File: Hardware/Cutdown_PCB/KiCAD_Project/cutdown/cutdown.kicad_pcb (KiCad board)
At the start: 4 copper layers, 43.2 x 152.4 mm, 74 parts, among them J1 Mini_USB_B, J2 External Cutdown, J3 ISP, J4 Hot Wire, Q1 2N7002, Q2 FQP30N06L, SW1 SW_SPST, U1 FT231XS, U2 SPX3819M5-L-3-3, U3 ATmega328P-AU, U4 XBee, U5 BMP388, Y1 8MHz

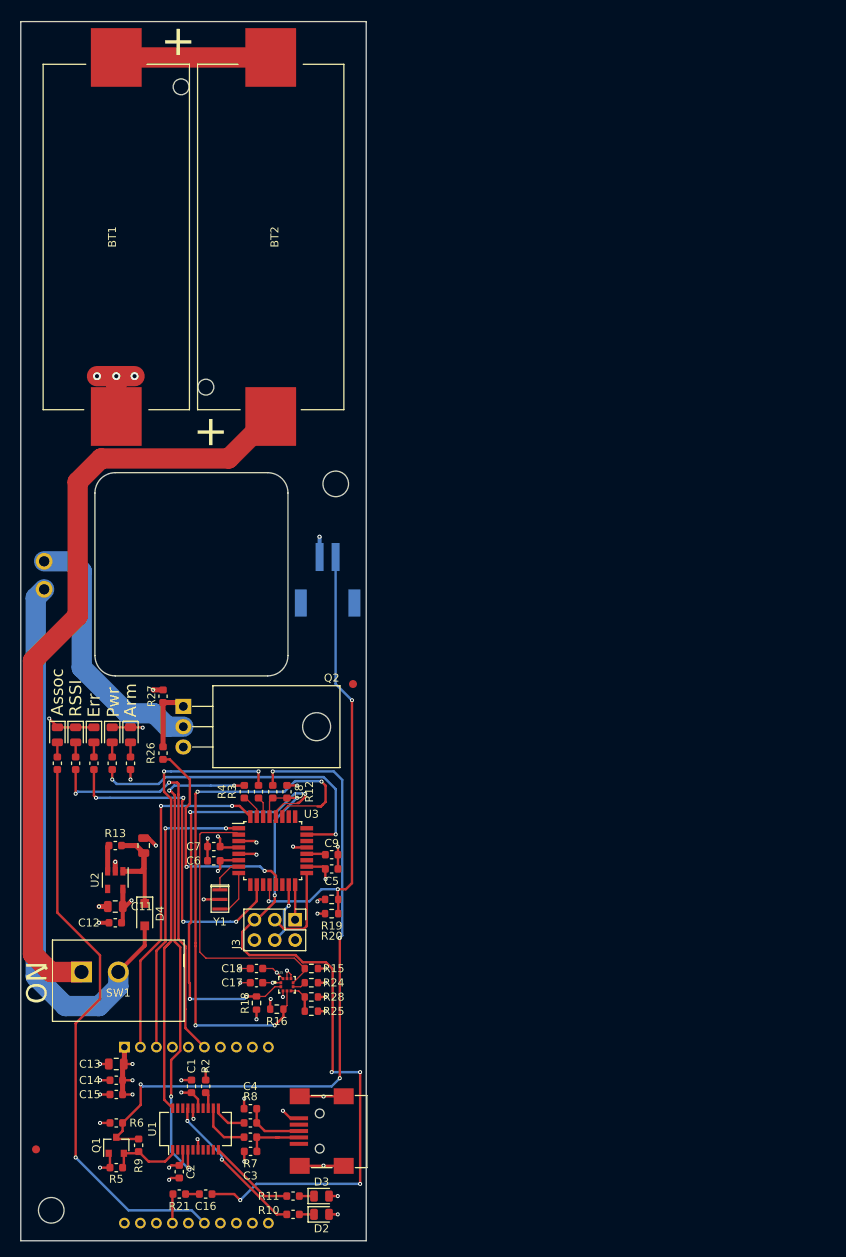
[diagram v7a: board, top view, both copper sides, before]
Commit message: Add Arm LED and improve board layout
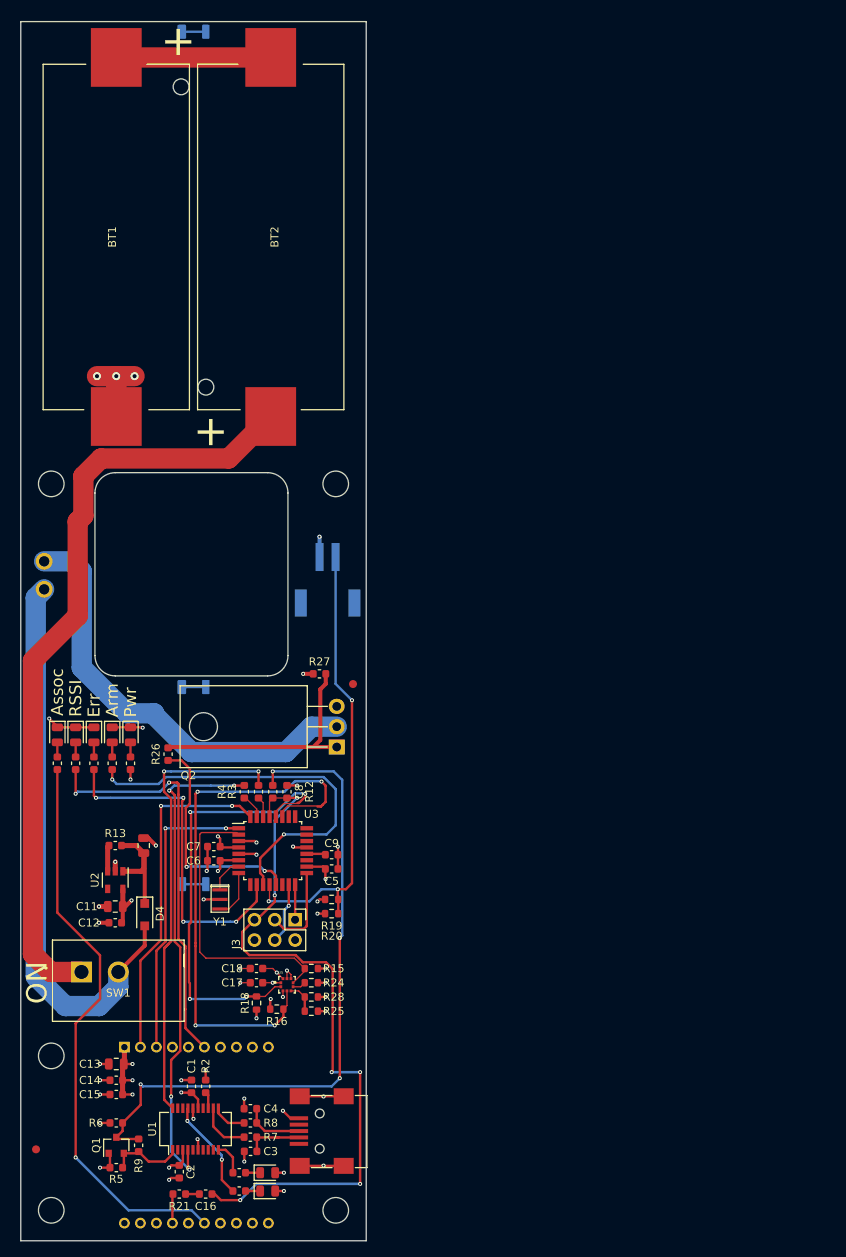
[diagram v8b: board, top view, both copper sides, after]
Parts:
- added H3: M3_ISO_7380, mechanical:MountingHole_3.2mm_M3_ISO7380, F.Cu at (105.9, 82.9)
- added H4: M3_ISO_7380, mechanical:MountingHole_3.2mm_M3_ISO7380, F.Cu at (141.5, 173.7)
- added H5: M3_ISO_7380, mechanical:MountingHole_3.2mm_M3_ISO7380, F.Cu at (105.9, 154.4)
- added TP1: 1-0000952, test_points:1-0000952, B.Cu at (123.7, 26.4)
- added TP2: 1-0000952, test_points:1-0000952, B.Cu at (123.7, 79.8)
- added TP3: 1-0000952, test_points:1-0000952, B.Cu at (123.7, 133.0)
- added TP4: 1-0000952, test_points:1-0000952, B.Cu at (123.7, 108.3)
- moved Q2 19.8 mm to (141.6, 115.8), turned to 90 degrees
- moved R27 19.8 mm to (139.4, 106.7), turned to 180 degrees
- moved D2 7.34 mm to (133.0, 171.3)
- moved D3 7.34 mm to (133.0, 169.0)
- moved R10 7.34 mm to (129.4, 171.3)
- moved R11 7.34 mm to (129.4, 169.0)
- moved R26 0.65 mm to (120.5, 116.7)
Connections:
- U3 pad 11: (no net) -> Net-(R14-Pad2)
- U3 pad 23: Net-(R14-Pad2) -> (no net)
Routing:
- net Net-(Q2-Pad1): track 8.28 -> 53.4 mm
- net Net-(J4-Pad2): track 33.0 -> 54.9 mm
- net Net-(R14-Pad2): track 39.7 -> 49.5 mm
- net Net-(R11-Pad2): track 10.9 -> 4.13 mm
- net Net-(R10-Pad2): track 19.2 -> 12.8 mm
- net Net-(TP4-Pad1): track 0.00 -> 3.00 mm
- net Net-(TP3-Pad1): track 0.00 -> 3.00 mm
- net Net-(TP2-Pad1): track 0.00 -> 3.00 mm
- net Net-(TP1-Pad1): track 0.00 -> 3.00 mm
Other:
- board text removed: "BATT"
